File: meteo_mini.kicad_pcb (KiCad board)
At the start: 2 copper layers, 50 x 18 mm, 15 parts, among them J1 Conn_01x04, J2 Conn_01x06, J3 Conn_01x04, J4 USB_A, SW1 SW_SPST, U1 STM32F103C8T6, U2 XC6206PxxxMR

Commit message: new pcb design is coming
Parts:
- removed J2: Conn_01x06, Connector_PinHeader_2.54mm:PinHeader_1x06_P2.54mm_Vertical
- added C7: 1u, Capacitor_SMD:C_0603_1608Metric, F.Cu at (99.0, 39.1)
- added C8: 0.1u, Capacitor_SMD:C_0603_1608Metric, F.Cu at (95.0, 39.1)
- added D1: LED, LED_SMD:LED_0603_1608Metric, F.Cu at (82.0, 45.7)
- added D2: LED, LED_SMD:LED_0603_1608Metric, F.Cu at (82.0, 43.1)
- added R3: 10k, Resistor_SMD:R_0603_1608Metric, F.Cu at (77.7, 47.7)
- added R4: 10k, Resistor_SMD:R_0603_1608Metric, F.Cu at (73.7, 48.3)
- added R5: 390, Resistor_SMD:R_0603_1608Metric, F.Cu at (102.4, 32.8)
- added R6: 390, Resistor_SMD:R_0603_1608Metric, F.Cu at (91.0, 39.1)
- added U3: BME280, Package_LGA:Bosch_LGA-8_2.5x2.5mm_P0.65mm_ClockwisePinNumbering, F.Cu at (78.0, 43.9)
- C4: footprint Capacitor_SMD:C_0805_2012Metric -> Capacitor_SMD:C_0603_1608Metric
- J4: moved to F.Cu
- SW1: footprint Button_Switch_SMD:SW_SPST_REED_CT05-XXXX-J1 -> Button_Switch_SMD:SW_SPST_PTS645
- moved C1 48.0 mm to (102.4, 35.3)
- moved R2 40.5 mm to (102.4, 27.8), turned to 0 degrees
- moved R1 39.0 mm to (102.4, 30.3), turned to 0 degrees
- moved C2 38.7 mm to (95.0, 44.1)
- moved C5 36.1 mm to (95.0, 41.6), turned to 0 degrees
- moved C4 26.9 mm to (91.0, 44.1), turned to 0 degrees
- moved C3 26.9 mm to (91.0, 46.6), turned to 0 degrees
- moved C6 26.0 mm to (91.0, 41.6), turned to 0 degrees
- moved SW1 16.1 mm to (98.5, 73.0), turned to 0 degrees
- moved U2 4.11 mm to (70.0, 72.0), turned to 0 degrees
- moved J1 2.56 mm to (108.0, 65.0)
- moved U1 2.20 mm to (85.0, 69.0), turned to 315 degrees
- moved J3 1.06 mm to (70.0, 62.0)
- moved J4 0.85 mm to (55.4, 69.0)
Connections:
- U1 pad 45: Net-(U1-Pad45) -> /LED
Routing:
- net +3V3: track 77.5 -> 0.00 mm
- net GND: track 66.4 -> 0.00 mm, vias 3 -> 0
- net /I2C1SCL: track 32.1 -> 0.00 mm
- net /I2C1SDA: track 30.3 -> 0.00 mm
- net /VDDBME: track 29.4 -> 0.00 mm, vias 1 -> 0
- net /SWDCLK: track 29.2 -> 0.00 mm, vias 1 -> 0
- net /SWDIO: track 19.9 -> 0.00 mm, vias 1 -> 0
- net +5V: track 17.3 -> 0.00 mm, vias 1 -> 0
- net /RESET: track 15.3 -> 0.00 mm
- net Net-(J4-Pad5): track 14.0 -> 0.00 mm
- net Net-(R1-Pad1): track 7.67 -> 0.00 mm
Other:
- board text removed: "LiZARD"

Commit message: Move components
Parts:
- SW1: footprint Button_Switch_SMD:SW_SPST_PTS645 -> Button_Switch_SMD:SW_SPST_FSMSM
- moved C5 52.6 mm to (69.5, 76.3)
- moved R6 44.9 mm to (93.3, 71.8)
- moved C6 38.9 mm to (69.5, 73.4)
- moved C7 34.7 mm to (89.6, 76.3), turned to 180 degrees
- moved C4 33.4 mm to (74.5, 68.0), turned to 270 degrees
- moved U1 29.4 mm to (101.1, 62.1), turned to 90 degrees
- moved C8 28.7 mm to (69.4, 65.5), turned to 180 degrees
- moved C3 27.7 mm to (77.0, 68.0), turned to 270 degrees
- moved U3 2.67 mm to (69.7, 69.3), turned to 180 degrees
- moved SW1 2.06 mm to (97.8, 74.9)
- turned U2 to 135 degrees
- renumbered C7 to C1, C8 to C2, C4 to C3, C5 to C4, C1 to C5, C2 to C6, C6 to C7, C3 to C8, J4 to J1, J3 to J2, J1 to J3, R3 to R1, R4 to R2, R5 to R3, R6 to R4, R1 to R5, R2 to R6, U3 to U1, U1 to U2, U2 to U3
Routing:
- removed copper zone on B.Cu, net GND

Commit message: First version
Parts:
- J1: moved to B.Cu
- moved R5 50.1 mm to (76.2, 73.0), turned to 180 degrees
- moved R4 40.0 mm to (76.2, 76.3), turned to 180 degrees
- moved R2 36.3 mm to (102.4, 70.4)
- moved R3 35.7 mm to (93.3, 67.3)
- moved D2 33.2 mm to (80.9, 76.3)
- moved R1 31.6 mm to (102.4, 67.3)
- moved C2 31.4 mm to (97.5, 70.4), turned to 180 degrees
- moved C1 28.2 mm to (97.5, 67.3), turned to 180 degrees
- moved D1 21.7 mm to (93.3, 64.3)
- moved C4 2.49 mm to (76.2, 66.2), turned to 180 degrees
- moved J3 2.38 mm to (107.2, 62.8)
- moved U1 1.66 mm to (102.4, 63.1)
- moved R6 1.36 mm to (93.3, 70.4)
- moved C3 1.31 mm to (76.2, 69.1), turned to 180 degrees
- moved C8 0.60 mm to (69.9, 65.9)
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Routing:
- net +3V3: track 0.00 -> 121.3 mm
- net GND: track 0.00 -> 77.3 mm, vias 0 -> 8
- net /I2C1SDA: track 0.00 -> 54.4 mm, vias 0 -> 3
- net /I2C1SCL: track 0.00 -> 50.5 mm, vias 0 -> 3
- net +5V: track 0.00 -> 21.2 mm, vias 0 -> 1
- net /SWDCLK: track 0.00 -> 16.2 mm, vias 0 -> 1
- net /RESET: track 0.00 -> 14.7 mm
- net /SWDIO: track 0.00 -> 13.1 mm, vias 0 -> 1
- net Net-(R5-Pad1): track 0.00 -> 5.74 mm
- net /LED: track 0.00 -> 4.18 mm
- net Net-(D2-Pad1): track 0.00 -> 3.12 mm
- net Net-(D1-Pad1): track 0.00 -> 3.00 mm
- added copper zone on B.Cu, net GND
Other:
- net class Default: clearance 0.1524 -> 0.05
- rule trace_clearance: 0.1524 -> 0.05
- rule trace_min: 0.1524 -> 0.0524

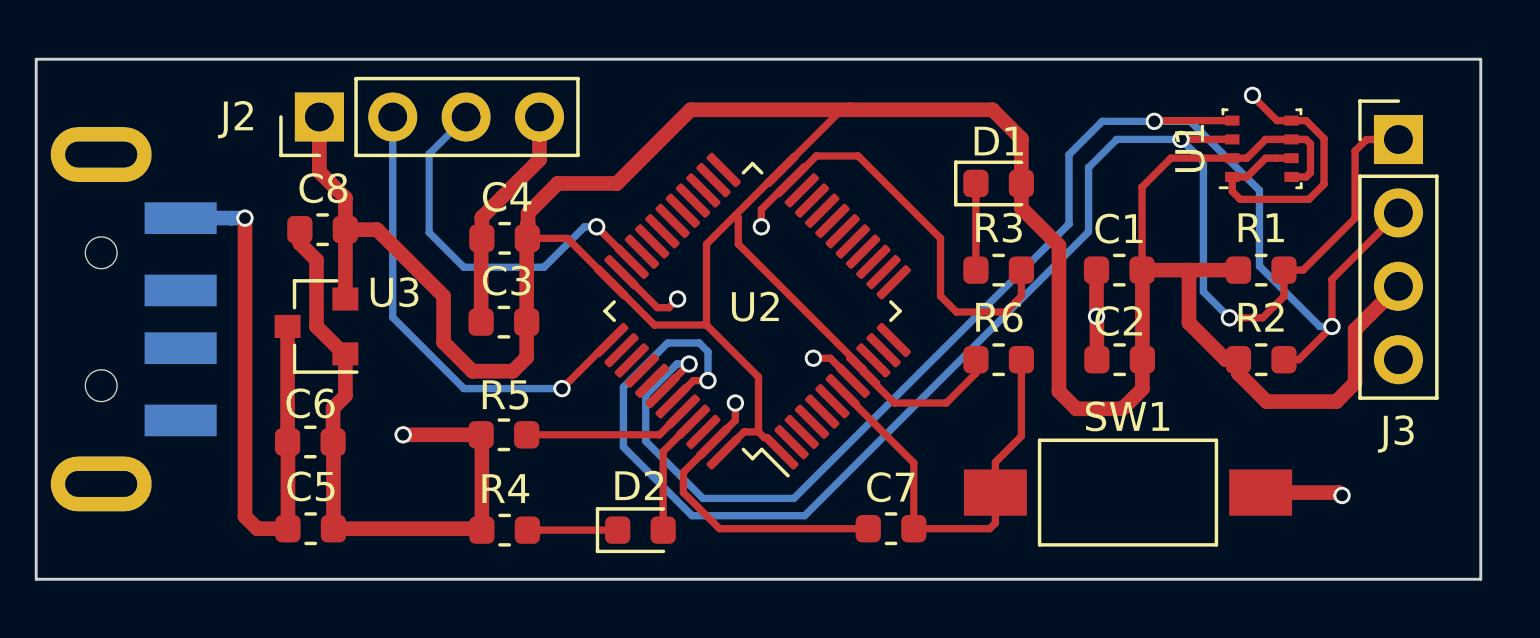
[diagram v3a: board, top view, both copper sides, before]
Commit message: Ground polygone under MCU, Vcc though via
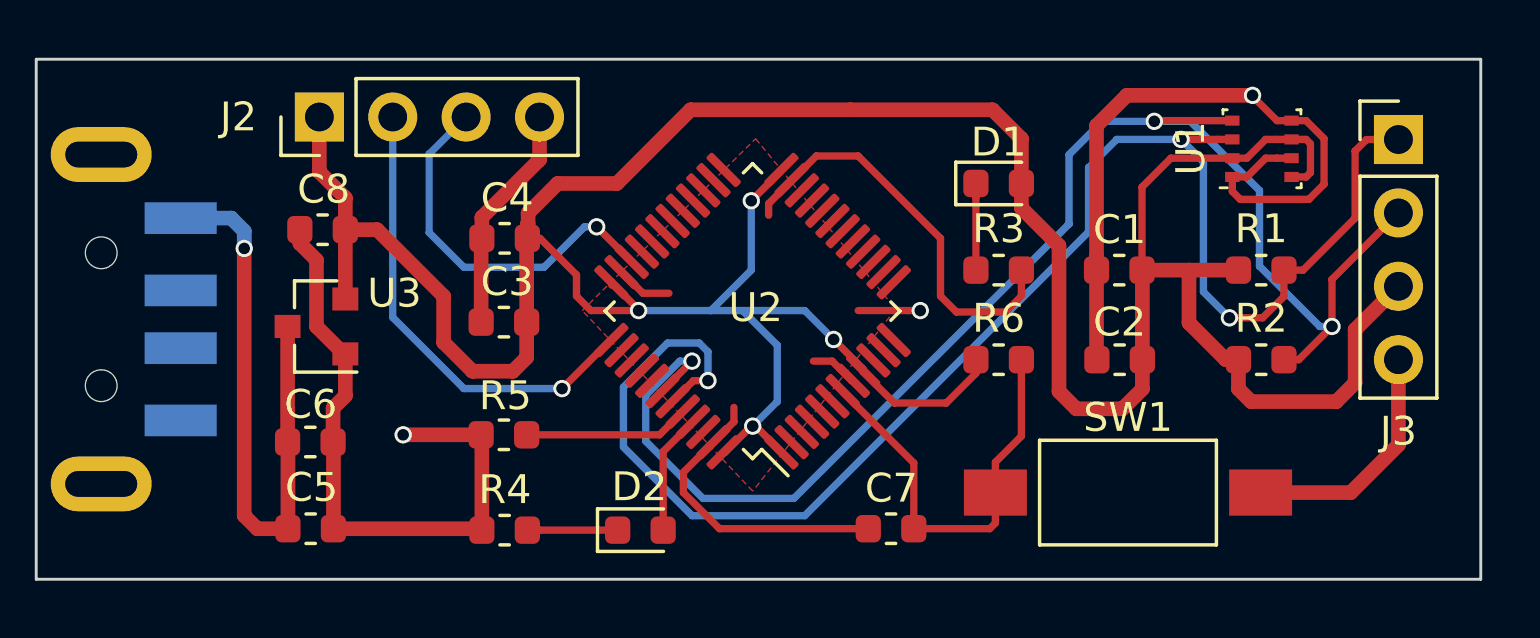
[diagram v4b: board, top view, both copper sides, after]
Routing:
- net GND: track 77.3 -> 94.9 mm, vias 8 -> 3
- net +3V3: track 121.3 -> 119.5 mm, vias 0 -> 4
- added copper zone on F.Cu, net GND

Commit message: New PCB production
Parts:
- moved J1 35.0 mm to (77.0, 41.5)
- moved C2 34.4 mm to (118.2, 42.9)
- moved C8 34.4 mm to (90.6, 38.4)
- moved R2 34.4 mm to (123.0, 42.9)
- moved R6 34.4 mm to (114.0, 42.9)
- moved C1 34.4 mm to (118.1, 39.8)
- moved C3 34.4 mm to (96.8, 41.6)
- moved C5 34.4 mm to (90.2, 48.8)
- moved C6 34.4 mm to (90.1, 45.8)
- moved D1 34.4 mm to (114.0, 36.8)
- moved D2 34.4 mm to (101.6, 48.8)
- moved J2 34.4 mm to (90.5, 34.5)
- moved R3 34.4 mm to (114.0, 39.8)
- moved R5 34.4 mm to (96.8, 45.5)
- moved U1 34.4 mm to (123.1, 35.6)
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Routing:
- net +5V: track 20.9 -> 25.5 mm
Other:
- board text added: "optim"
